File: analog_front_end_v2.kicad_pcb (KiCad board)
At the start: 4 copper layers, 101 parts, among them J1 Conn_Coaxial, J3 Conn_01x01_Socket, J4 Conn_01x01_Socket, U1 ADL5531, U10 MAX6002, U11 LP2985-5.0, U12 MAX2606, U13 PAT1220-C-0DB, U14 LP2985-5.0, U15 BFP540ESD, U16 BFP540ESD, U17 LP2985-3.3, U18 PAT1220-C-0DB, U19 PAT1220-C-0DB, U2 ADL5531, U20 PAT1220-C-0DB, U21 PAT1220-C-0DB, U3 ADL5531, U4 ADL5531, U5 LP2985-1.8, U6 MCP33131, U7 PAT1220-C-0DB, U8 ADL5531, U9 PMOD 2x6

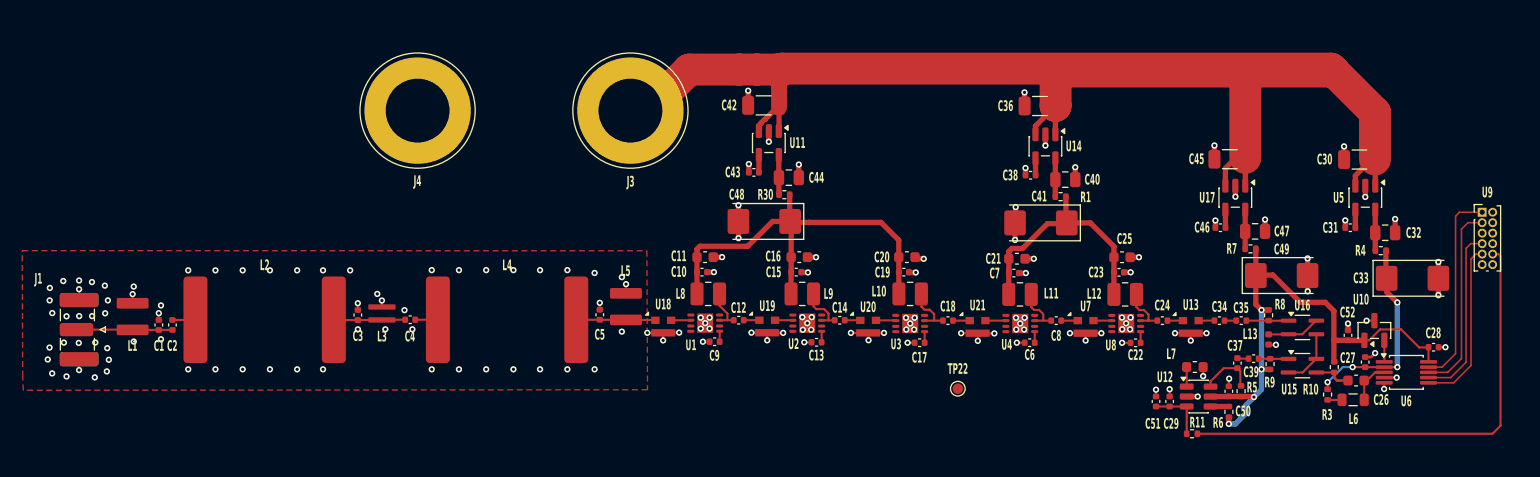
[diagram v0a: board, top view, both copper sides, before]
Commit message: Further PCB touchups ready for manufacturing
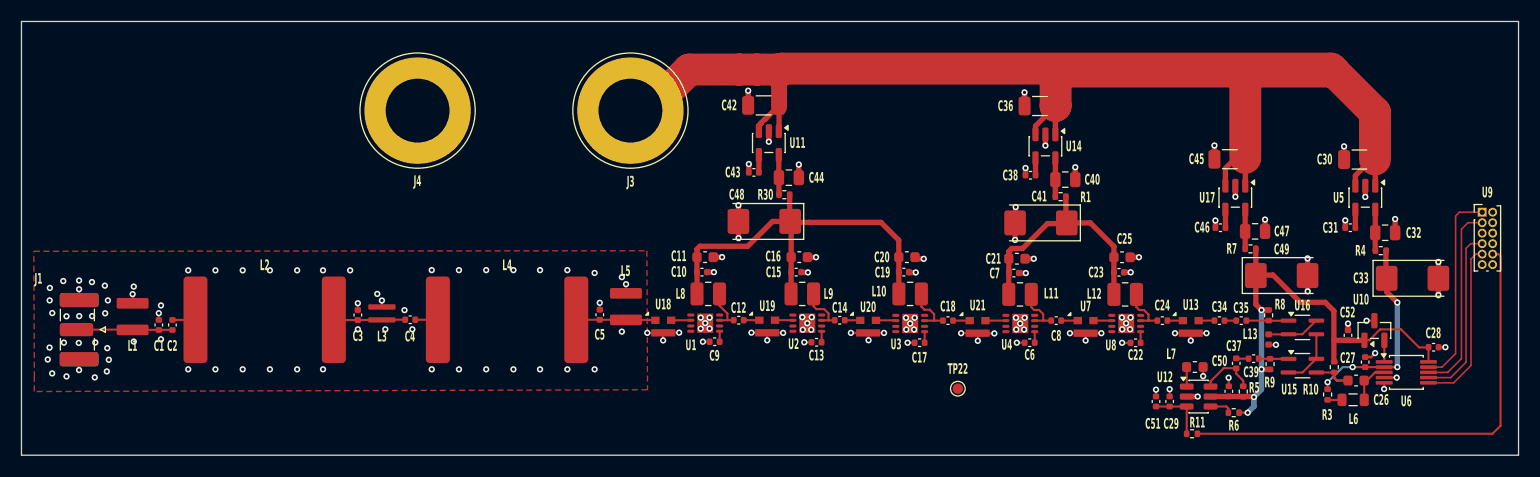
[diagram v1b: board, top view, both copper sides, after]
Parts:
- moved R6 0.47 mm to (128.7, 49.3), turned to 0 degrees
- moved R5 0.21 mm to (129.6, 47.3)
- moved C37 0.11 mm to (129.0, 44.6)
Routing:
- net 3V3: track 50.4 -> 48.4 mm
- net Net-(U12-OUT-): track 1.50 -> 2.18 mm
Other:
- board outline added: 142.9 x 41.4 mm
